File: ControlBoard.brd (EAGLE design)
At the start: 100 x 100 mm, 0 parts

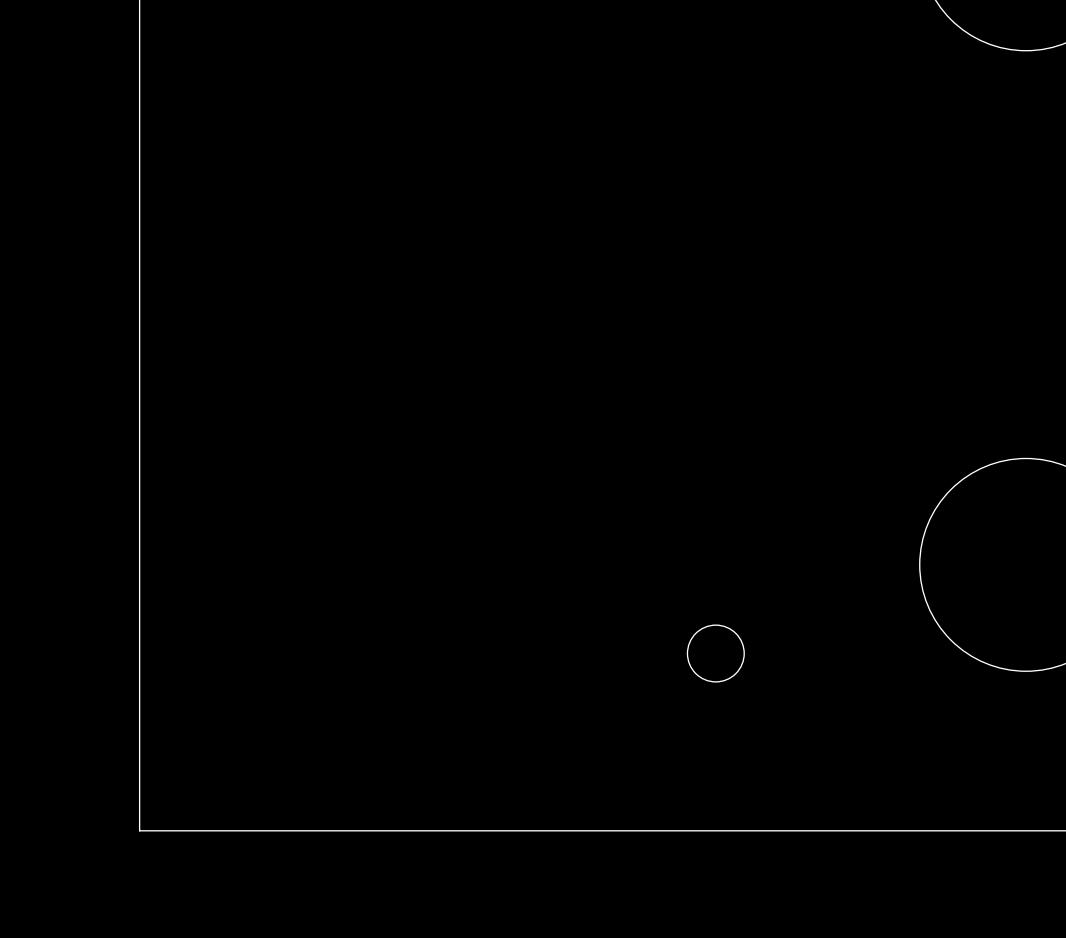
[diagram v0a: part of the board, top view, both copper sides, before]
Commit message: Added MCU and joystick to schematic.
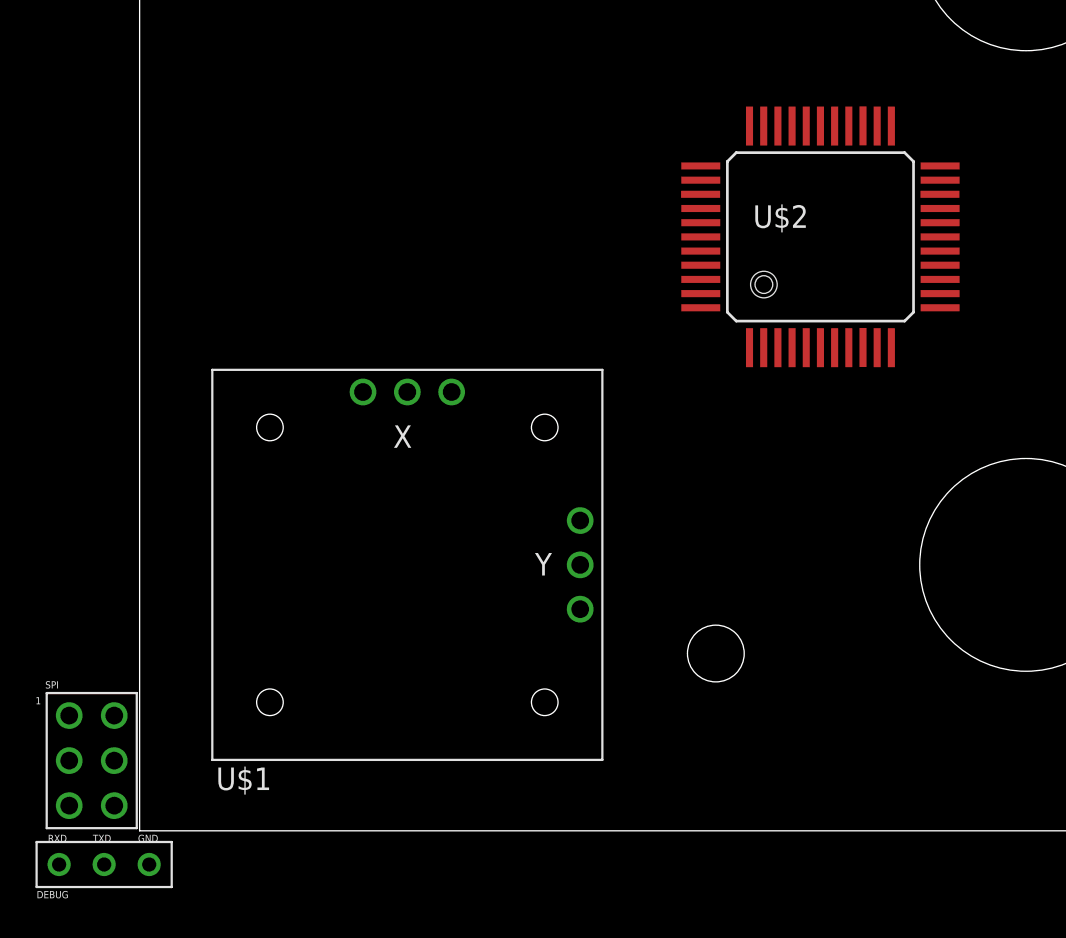
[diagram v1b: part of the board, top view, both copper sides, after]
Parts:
- added DEBUG: CONNECTOR_3PINUSART, connectors:1X3_USART
- added SPI: CONNECTOR_6PIN2X3_ISP, connectors:2X3_ISP
- added U$1: JOYSTIC-XYRKJXK122000D, jogwheelParts:JOYSTICK-RKJXK122000D
- added U$2: ATMEGA[164/324/644/644][A/PA]TQFP/QFN/MLF, jogwheelParts:QFP-44
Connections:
- new net !RESET: SPI.RST, U$2.4
- new net N$1: U$1.X3, U$1.Y3
- new net N$2: U$1.X1, U$1.Y1
- new net N$3: SPI.V+
- new net N$4: DEBUG.GND, SPI.GND
- new net N$5: U$2.17, U$2.38, U$2.5
- new net PORTA0: U$1.Y2, U$2.37
- new net PORTA1: U$1.X2, U$2.36
- new net PORTA2: U$2.35
- new net PORTA3: U$2.34
- new net PORTA4: U$2.33
- new net PORTA5: U$2.32
- new net PORTA6: U$2.31
- new net PORTA7: U$2.30
- new net PORTB0: U$2.40
- new net PORTB1: U$2.41
- new net PORTB2: U$2.42
- new net PORTB3: U$2.43
- new net PORTB4: U$2.44
- new net PORTB5: SPI.MOSI, U$2.1
- new net PORTB6: SPI.MISO, U$2.2
- new net PORTB7: SPI.SCK, U$2.3
- new net PORTC0: U$2.19
- new net PORTC1: U$2.20
- new net PORTC2: U$2.21
- new net PORTC3: U$2.22
- new net PORTC4: U$2.23
- new net PORTC5: U$2.24
- new net PORTC6: U$2.25
- new net PORTC7: U$2.26
- new net PORTD0: DEBUG.TXD, U$2.9
- new net PORTD1: DEBUG.RXD, U$2.10
- new net PORTD2: U$2.11
- new net PORTD3: U$2.12
- new net PORTD4: U$2.13
- new net PORTD5: U$2.14
- new net PORTD6: U$2.15
- new net PORTD7: U$2.16
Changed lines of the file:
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@@
 <layers>
 <layer number="1" name="Top" color="4" fill="1" visible="yes" active="yes"/>
+<layer number="2" name="Route2" color="1" fill="3" visible="no" active="yes"/>
+<layer number="15" name="Route15" color="4" fill="6" visible="no" active="yes"/>
 <layer number="16" name="Bottom" color="1" fill="1" visible="yes" active="yes"/>
 <layer number="17" name="Pads" color="2" fill="1" visible="yes" active="yes"/>
@@
 <layer number="51" name="tDocu" color="7" fill="1" visible="yes" active="yes"/>
 <layer number="52" name="bDocu" color="7" fill="1" visible="yes" active="yes"/>
+<layer number="91" name="Nets" color="2" fill="1" visible="no" active="no"/>
+<layer number="92" name="Busses" color="1" fill="1" visible="no" active="no"/>
+<layer number="93" name="Pins" color="2" fill="1" visible="no" active="no"/>
+<layer number="94" name="Symbols" color="4" fill="1" visible="no" active="no"/>
+<layer number="95" name="Names" color="7" fill="1" visible="no" active="no"/>
+<layer number="96" name="Values" color="7" fill="1" visible="no" active="no"/>
+<layer number="97" name="Info" color="7" fill="1" visible="no" active="no"/>
+<layer number="98" name="Guide" color="6" fill="1" visible="no" active="no"/>
 <layer number="100" name="PART_LOCATIONS" color="13" fill="1" visible="yes" active="yes"/>
 </layers>
@@
 </autorouter>
 <elements>
+<element name="U$1" library="jogwheelParts" package="JOYSTICK-RKJXK122000D" value="JOYSTIC-XYRKJXK122000D" x="15.1" y="15">
+<attribute name="SECOND-AXIS" value="Y" x="15.1" y="15" size="1.778" layer="27" font="vector" display="off"/>
+<attribute name="FIRST-AXIS" value="X" x="15.1" y="15" size="1.778" layer="27" font="vector" display="off"/>
+</element>
+<element name="U$2" library="jogwheelParts" package="QFP-44" value="ATMEGA[164/324/644/644][A/PA]TQFP/QFN/MLF" x="38.4" y="33.5"/>
+<element name="SPI" library="connectors" package="2X3_ISP" value="CONNECTOR_6PIN2X3_ISP" x="-2.7" y="6.5"/>
+<element name="DEBUG" library="connectors" package="1X3_USART" value="CONNECTOR_3PINUSART" x="-2" y="-1.9">
+<attribute name="PIN1" value="TXD" x="-2" y="-1.9" size="1.778" layer="27" display="off"/>
+<attribute name="PIN2" value="RXD" x="-2" y="-1.9" size="1.778" layer="27" display="off"/>
+<attribute name="PIN3" value="GND" x="-2" y="-1.9" size="1.778" layer="27" display="off"/>
+</element>
 </elements>
 <signals>
+<signal name="PORTD0">
+<contactref element="U$2" pad="9"/>
+<contactref element="DEBUG" pad="TXD"/>
+<wire x1="-2" y1="-1.9" x2="40.8" y2="27.26" width="0" layer="19" extent="1-1"/>
+</signal>
+<signal name="PORTD1">
+<contactref element="U$2" pad="10"/>
+<contactref element="DEBUG" pad="RXD"/>
+<wire x1="-4.54" y1="-1.9" x2="41.6" y2="27.25" width="0" layer="19" extent="1-1"/>
+</signal>
+<signal name="PORTD2">
+<contactref element="U$2" pad="11"/>
+</signal>
+<signal name="PORTD3">
+<contactref element="U$2" pad="12"/>
+</signal>
+<signal name="PORTD4">
+<contactref element="U$2" pad="13"/>
+</signal>
+<signal name="PORTD5">
+<contactref element="U$2" pad="14"/>
+</signal>
+<signal name="PORTD6">
+<contactref element="U$2" pad="15"/>
+</signal>
+<signal name="PORTD7">
+<contactref element="U$2" pad="16"/>
+</signal>
+<signal name="PORTC0">
+<contactref element="U$2" pad="19"/>
+</signal>
+<signal name="PORTC1">
+<contactref element="U$2" pad="20"/>
+</signal>
+<signal name="PORTC2">
+<contactref element="U$2" pad="21"/>
+</signal>
+<signal name="PORTC3">
+<contactref element="U$2" pad="22"/>
+</signal>
+<signal name="PORTC4">
+<contactref element="U$2" pad="23"/>
+</signal>
+<signal name="PORTC5">
+<contactref element="U$2" pad="24"/>
+</signal>
+<signal name="PORTC6">
+<contactref element="U$2" pad="25"/>
+</signal>
+<signal name="PORTC7">
+<contactref element="U$2" pad="26"/>
+</signal>
+<signal name="PORTA0">
+<contactref element="U$2" pad="37"/>
+<contactref element="U$1" pad="Y2"/>
+<wire x1="24.85" y1="15" x2="31.65" y2="35.1" width="0" layer="19" extent="1-1"/>
+</signal>
+<signal name="PORTA1">
+<contactref element="U$2" pad="36"/>
+<contactref element="U$1" pad="X2"/>
+<wire x1="15.1" y1="24.75" x2="31.64" y2="35.9" width="0" layer="19" extent="1-1"/>
+</signal>
+<signal name="PORTA2">
+<contactref element="U$2" pad="35"/>
+</signal>
+<signal name="PORTA3">
+<contactref element="U$2" pad="34"/>
+</signal>
+<signal name="PORTA4">
+<contactref element="U$2" pad="33"/>
+</signal>
+<signal name="PORTA5">
+<contactref element="U$2" pad="32"/>
+</signal>
+<signal name="PORTA6">
+<contactref element="U$2" pad="31"/>
+</signal>
+<signal name="PORTA7">
+<contactref element="U$2" pad="30"/>
+</signal>
+<signal name="PORTB0">
+<contactref element="U$2" pad="40"/>
+</signal>
+<signal name="PORTB1">
+<contactref element="U$2" pad="41"/>
+</signal>
+<signal name="PORTB2">
+<contactref element="U$2" pad="42"/>
+</signal>
+<signal name="PORTB3">
+<contactref element="U$2" pad="43"/>
+</signal>
+<signal name="PORTB4">
+<contactref element="U$2" pad="44"/>
+</signal>
+<signal name="PORTB5">
+<contactref element="U$2" pad="1"/>
+<contactref element="SPI" pad="MOSI"/>
+<wire x1="-1.43" y1="3.96" x2="34.4" y2="27.25" width="0" layer="19" extent="1-1"/>
+</signal>
+<signal name="PORTB6">
+<contactref element="U$2" pad="2"/>
+<contactref element="SPI" pad="MISO"/>
+<wire x1="-3.97" y1="6.5" x2="35.2" y2="27.25" width="0" layer="19" extent="1-1"/>
+</signal>
+<signal name="N$1">
+<contactref element="U$1" pad="Y3"/>
+<contactref element="U$1" pad="X3"/>
+<wire x1="24.85" y1="12.5" x2="17.6" y2="24.75" width="0" layer="19" extent="1-1"/>
+</signal>
+<signal name="N$2">
+<contactref element="U$1" pad="Y1"/>
+<contactref element="U$1" pad="X1"/>
+<wire x1="12.6" y1="24.75" x2="24.85" y2="17.5" width="0" layer="19" extent="1-1"/>
+</signal>
+<signal name="!RESET">
+<contactref element="U$2" pad="4"/>
+<contactref element="SPI" pad="RST"/>
+<wire x1="-3.97" y1="1.42" x2="36.8" y2="27.25" width="0" layer="19" extent="1-1"/>
+</signal>
+<signal name="PORTB7">
+<contactref element="SPI" pad="SCK"/>
+<contactref element="U$2" pad="3"/>
+<wire x1="-3.97" y1="3.96" x2="36" y2="27.25" width="0" layer="19" extent="1-1"/>
+</signal>
+<signal name="N$3">
+<contactref element="SPI" pad="V+"/>
+</signal>
+<signal name="N$4">
+<contactref element="SPI" pad="GND"/>
+<contactref element="DEBUG" pad="GND"/>
+<wire x1="0.54" y1="-1.9" x2="-1.43" y2="1.42" width="0" layer="19" extent="1-1"/>
+</signal>
+<signal name="N$5">
+<contactref element="U$2" pad="38"/>
+<contactref element="U$2" pad="17"/>
+<contactref element="U$2" pad="5"/>
+<wire x1="37.6" y1="27.25" x2="45.15" y2="33.5" width="0" layer="19" extent="1-1"/>
+<wire x1="31.65" y1="34.3" x2="37.6" y2="27.25" width="0" layer="19" extent="1-1"/>
+</signal>
 </signals>
 </board>

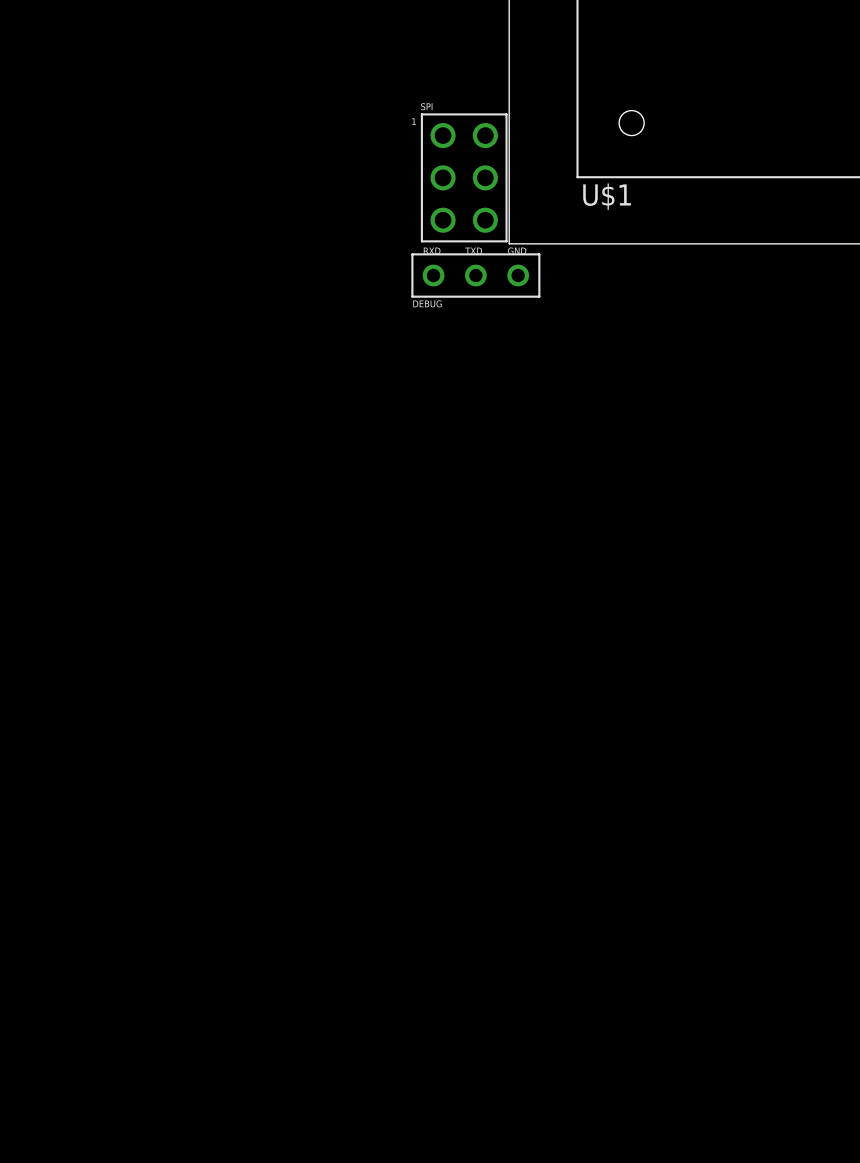
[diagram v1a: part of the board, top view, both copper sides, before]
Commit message: Added FT232 and button connectors.
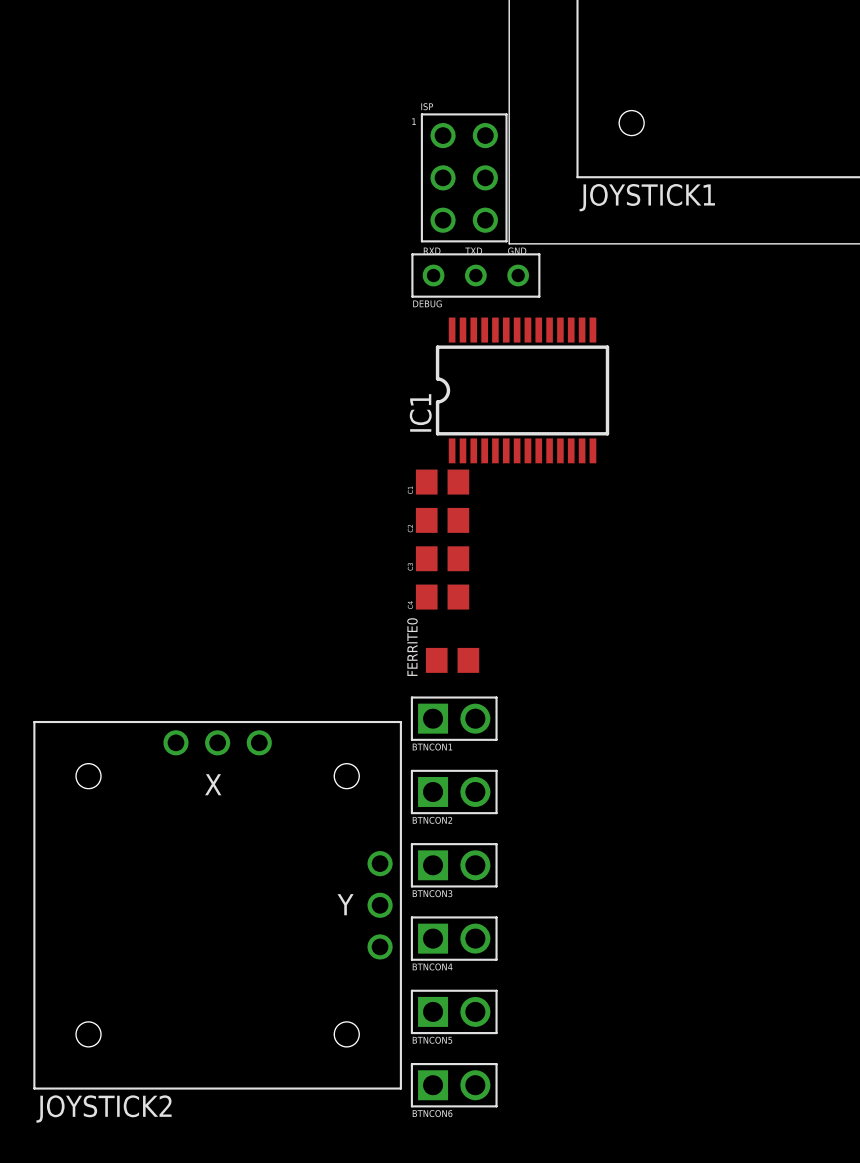
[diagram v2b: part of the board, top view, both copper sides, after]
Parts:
- added BTNCON1, BTNCON2, BTNCON3, BTNCON4, BTNCON5, BTNCON6: CONNECTOR_2PIN1X2_WIRE, connectors:1X2_WIRE
- added C1, C2, C3: 100nF, RC_and_L:C0805
- added C4: 10nF, RC_and_L:C0805
- added FERRITE0: (no value), RC_and_L:R0805
- added IC1: FT232RL, jogwheelParts:SSOP28
- added JOYSTICK2: JOYSTIC-XYRKJXK122000D, jogwheelParts:JOYSTICK-RKJXK122000D
- renumbered SPI to ISP, U$1 to JOYSTICK1
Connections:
- removed net N$1: JOYSTICK1.X3, JOYSTICK1.Y3
- removed net N$4: DEBUG.GND, ISP.GND
- removed net N$5: U$2.17, U$2.38, U$2.5
- new net +5V: C2.1, C4.1, FERRITE0.2, IC1.20, IC1.4, ISP.V+, JOYSTICK1.X1, JOYSTICK1.Y1, JOYSTICK2.X1, JOYSTICK2.Y1, U$2.17, U$2.38, U$2.5
- new net GND: BTNCON1.1, BTNCON2.1, BTNCON3.1, BTNCON4.1, BTNCON5.1, BTNCON6.1, C1.2, C2.2, C3.1, C3.2, C4.2, DEBUG.GND, IC1.18, IC1.21, IC1.25, IC1.26, IC1.7, ISP.GND, JOYSTICK1.X3, JOYSTICK1.Y3, JOYSTICK2.X3, JOYSTICK2.Y3, U$2.18, U$2.28, U$2.39, U$2.6
- new net N$10: C1.1, IC1.17
- new net N$6: IC1.15
- new net N$7: IC1.16
- new net N$8: FERRITE0.1
- net N$2: now also IC1.23; no longer JOYSTICK1.X1, JOYSTICK1.Y1
- net N$3: now also IC1.22; no longer ISP.V+
- net PORTA2: now also JOYSTICK2.Y2
- net PORTA3: now also JOYSTICK2.X2
- net PORTC0: now also BTNCON1.2
- net PORTC1: now also BTNCON2.2
- net PORTC2: now also BTNCON3.2
- net PORTC3: now also BTNCON4.2
- net PORTC4: now also BTNCON5.2
- net PORTC5: now also BTNCON6.2
- net PORTD2: now also IC1.1
- net PORTD3: now also IC1.5

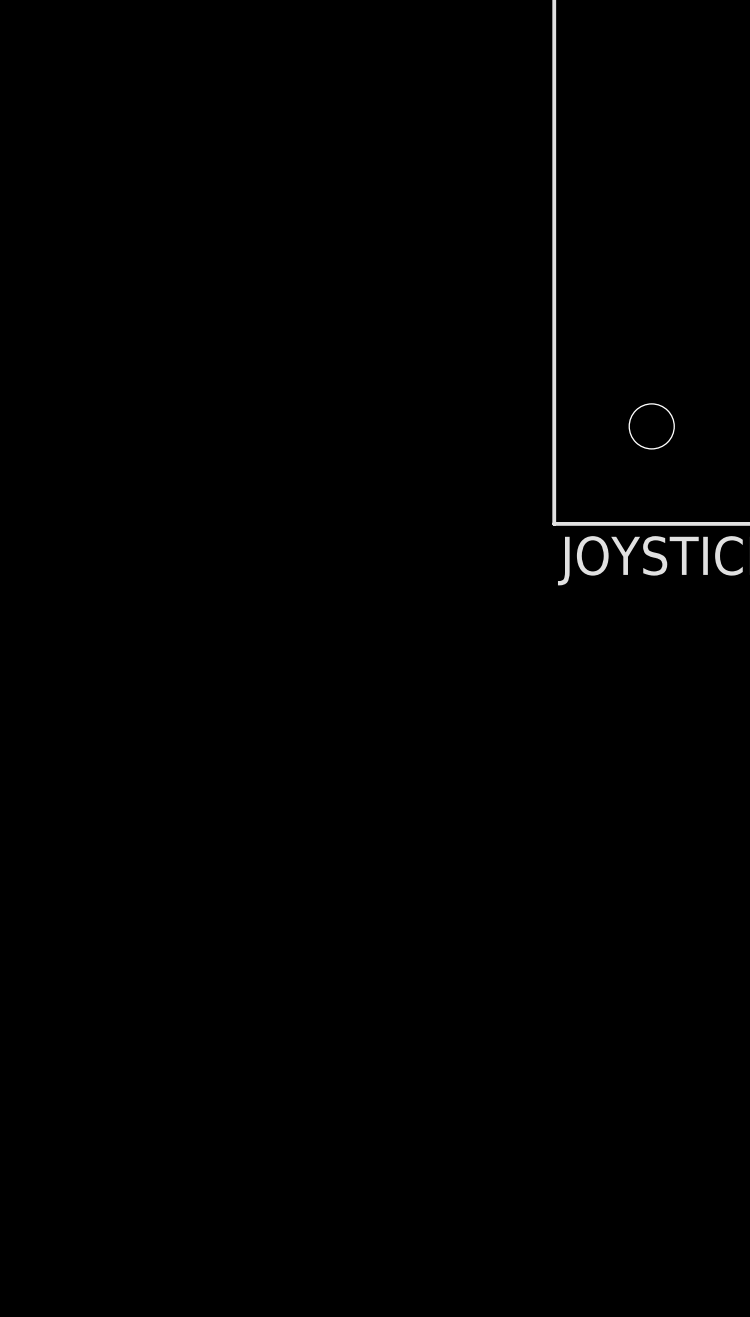
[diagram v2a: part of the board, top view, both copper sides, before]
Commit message: Added reference for ACD and USB connector.
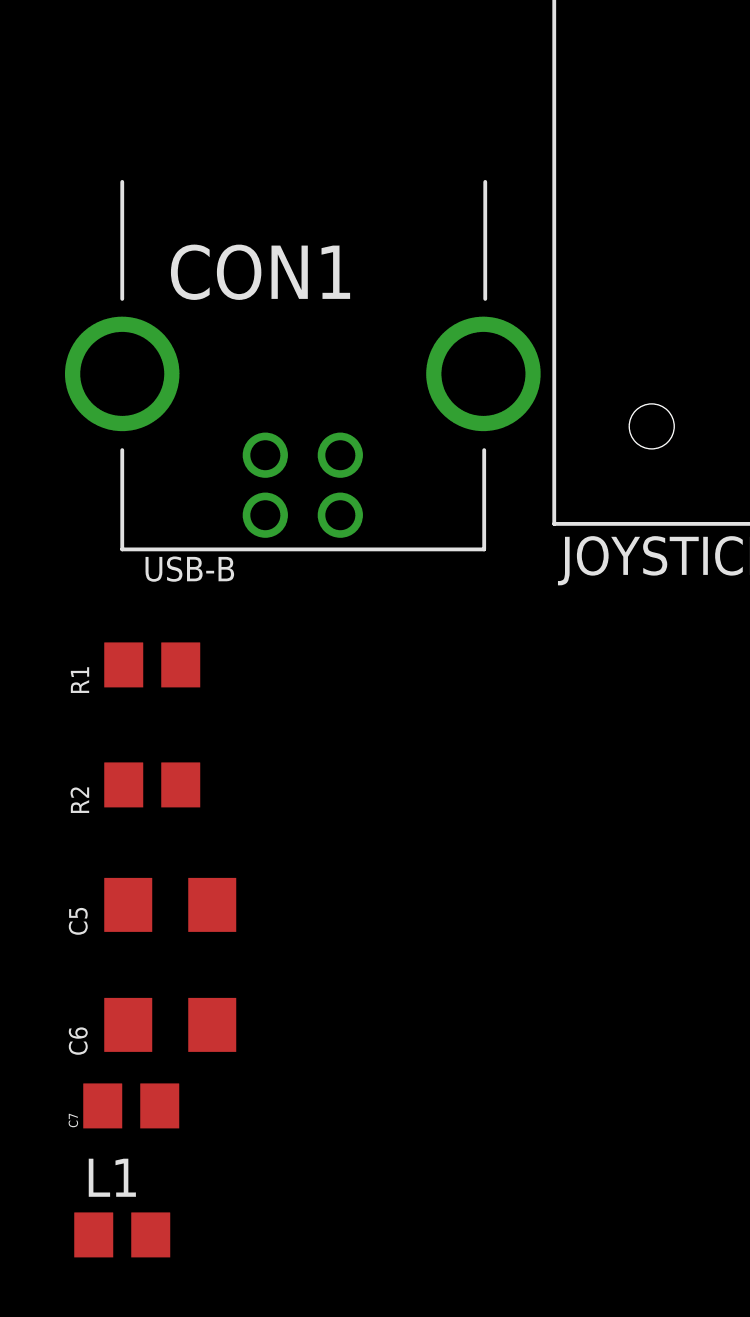
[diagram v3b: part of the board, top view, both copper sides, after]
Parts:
- added C5, C6: 22uF, RC_and_L:C1206
- added C7: 100nF, RC_and_L:C0805@1
- added CON1: USB-BWUERTH-ELECTRONIC-USB-B, jogwheelParts:USB-B-THROUGH-HOLE
- added L1: (no value), RC_and_L:C0805
- added R1, R2: 1k, RC_and_L:R0805
- C1, C2, C3, C4: device RC_and_L:C0805 -> RC_and_L:C0805@1
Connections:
- new net N$1: C7.2, U$2.27, U$2.29
- new net N$5: C7.1, L1.2
- net +5V: now also C3.1, C6.1, L1.1
- net GND: now also C6.2, CON1.GND, CON1.SHIELD, CON1.SHIELD@2; no longer C3.1
- net N$2: now also R1.1
- net N$3: now also R2.1
- net N$6: now also CON1.D+
- net N$7: now also CON1.D-
- net N$8: now also CON1.VCC
